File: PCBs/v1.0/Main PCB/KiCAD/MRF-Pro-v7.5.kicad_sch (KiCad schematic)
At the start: 4 parts, among them J1 Feather-1, J2 Feather-2, J3 FPC 8P Connector, J4 Conn_01x08

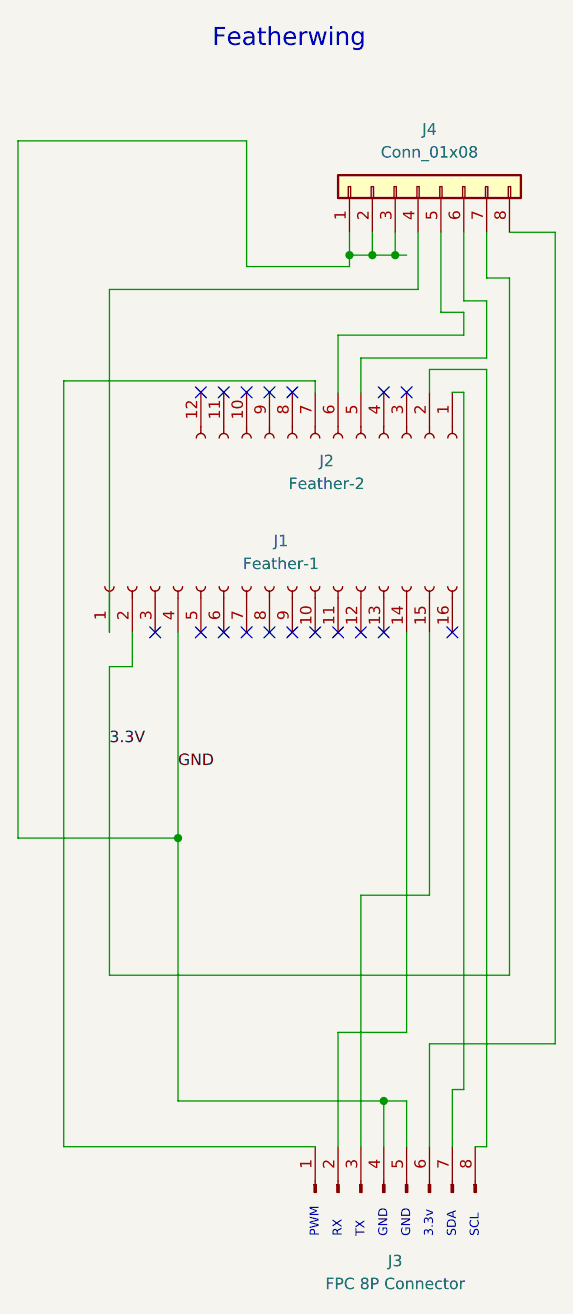
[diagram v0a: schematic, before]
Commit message: fix(pcb): put v7.5 FPC pin 1 on the switched rail instead of D11
FPC pin 1 ran to Feather D11, left over from a PWM experiment that was
never pursued. The breakout ties FPC pins 1 and 6 to the same 3.3 V net,
so the strap did nothing but reserve a GPIO and hang an unused pin on the
supply.

Pin 1 now joins pin 6 on 3V3_SW, the rail the J4 switch gates, so both
boards agree and the supply crosses the ribbon on two conductors instead
of one. D11 is free again. Boards already built are unaffected: they were
always powered through pin 6, and the firmware never drives D11.

ERC and DRC match the previous board exactly (same single wire-endpoint
warning, same 11 warnings, no unconnected pads). Zones refilled, Gerbers
and drill files re-plotted. Saving from KiCad 10 also upgrades the board
and project file format.

Docs and the v1 harness diagrams follow the change, and three stale J4
pin 7/8 references in the v8 errata now match the board.
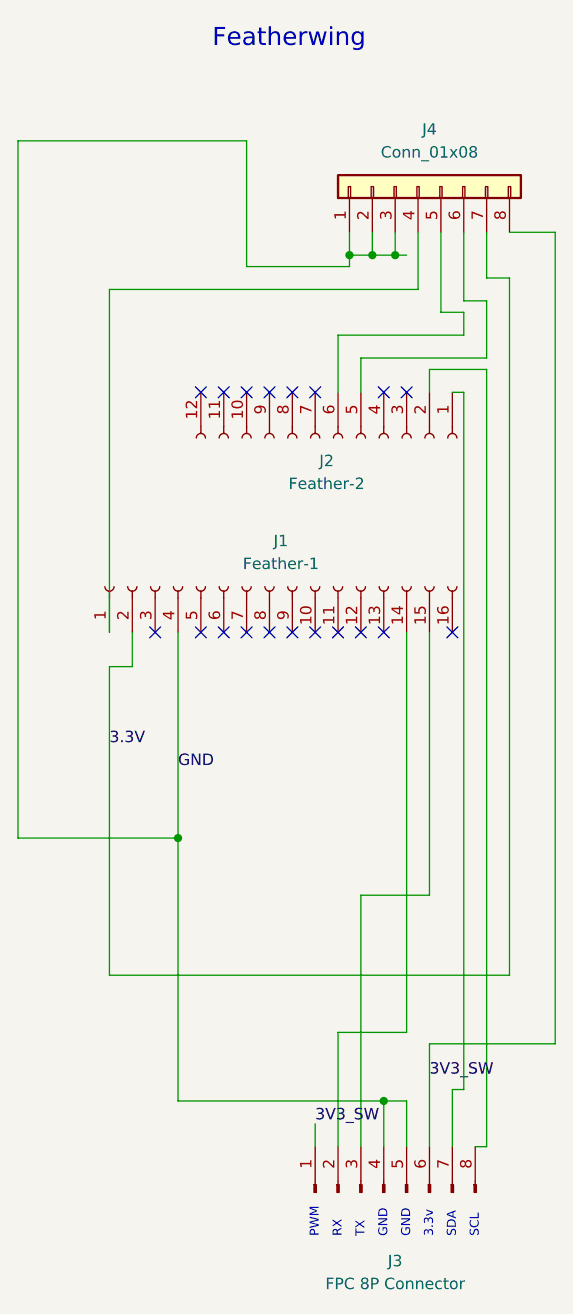
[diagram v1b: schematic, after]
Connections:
- net at J2.7 (Pin_7): no longer J3.1 (Pin_1)
- net 3V3_SW: now reaches J3.6 (Pin_6), J4.8 (Pin_8)
- net 3V3_SW: now also J3.1 (Pin_1)
- no-connect marks 18 -> 19
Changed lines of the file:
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@@
+	)
+	(no_connect
+		(at 92.71 72.39)
 	)
 	(no_connect
@@
 	(wire
 		(pts
-			(xy 64.77 71.12) (xy 64.77 156.21)
-		)
-		(stroke
-			(width 0)
-			(type default)
-		)
-	)
-	(wire
-		(pts
 			(xy 111.76 62.23) (xy 109.22 62.23)
 		)
@@
 	(wire
 		(pts
-			(xy 64.77 156.21) (xy 92.71 156.21)
-		)
-		(stroke
-			(width 0)
-			(type default)
-		)
-	)
-	(wire
-		(pts
 			(xy 114.3 137.16) (xy 114.3 59.69)
 		)
@@
 	(wire
 		(pts
-			(xy 92.71 72.39) (xy 92.71 71.12)
-		)
-		(stroke
-			(width 0)
-			(type default)
-		)
-	)
-	(wire
-		(pts
 			(xy 77.47 121.92) (xy 77.47 151.13)
 		)
@@
 	(wire
 		(pts
-			(xy 92.71 71.12) (xy 64.77 71.12)
-		)
-		(stroke
-			(width 0)
-			(type default)
-		)
-	)
-	(wire
-		(pts
 			(xy 119.38 144.78) (xy 119.38 54.61)
 		)
@@
 		)
 	)
+	(wire
+		(pts
+			(xy 92.71 156.21) (xy 92.71 153.67)
+		)
+		(stroke
+			(width 0)
+			(type default)
+		)
+	)
+	(label "3V3_SW"
+		(at 92.71 153.67 0)
+		(fields_autoplaced yes)
+		(effects
+			(font
+				(size 1.27 1.27)
+			)
+			(justify left bottom)
+		)
+		(property "Netclass" ""
+			(at 92.71 154.94 0)
+			(effects
+				(font
+					(size 1.27 1.27)
+					(italic yes)
+				)
+				(justify left)
+				(hide yes)
+			)
+		)
+	)
+	(label "3V3_SW"
+		(at 105.41 148.59 0)
+		(fields_autoplaced yes)
+		(effects
+			(font
+				(size 1.27 1.27)
+			)
+			(justify left bottom)
+		)
+		(property "Netclass" ""
+			(at 105.41 149.86 0)
+			(effects
+				(font
+					(size 1.27 1.27)
+					(italic yes)
+				)
+				(justify left)
+				(hide yes)
+			)
+		)
+	)
